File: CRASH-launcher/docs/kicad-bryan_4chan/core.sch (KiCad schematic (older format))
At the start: 22 parts, among them IC501 RFM12B, IC502 ATMEGA328P-PU, K501 CONN_3, K502 CONN_3, K503 CONN_3, P501 CONN_3X2, P502 TTL Serial / Prog, SW501 SW_PUSH, X501 8MHz

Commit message: 
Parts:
- removed L501: ANTENNA, symbol INDUCTOR
- removed SW501: SW_PUSH, symbol SW_PUSH
- added Antenna1: CONN_1, symbol CONN_1
- renumbered C501 to C10, C502 to C11, C503 to C12, C504 to C13, C505 to C14, C506 to C15, D501 to D7, D502 to D8, IC501 to IC1, IC502 to IC2, K501 to K1, K502 to K2, K503 to K3, P501 to P8, P502 to P9, R501 to R47, R502 to R48, R503 to R49, SP501 to SP1, X501 to X1
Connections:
- net labels removed: +3.3V
- no-connect marks 7 -> 6
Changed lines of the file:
@@
-EESchema Schematic File Version 2  date Mon 20 Feb 2012 05:21:35 PM MST
+EESchema Schematic File Version 2  date Sat 05 May 2012 12:12:20 AM MDT
 LIBS:bryan_custom
 LIBS:rfm12
@@
 $Descr User 11000 8500
 encoding utf-8
-Sheet 5 5
+Sheet 6 6
 Title ""
-Date "21 feb 2012"
+Date "13 apr 2012"
 Rev ""
 Comp ""
@@
 $EndDescr
 $Comp
-L SW_PUSH SW501
-U 1 1 4F25DF75
-P 3950 6500
-F 0 "SW501" H 4100 6610 50  0000 C CNN
-F 1 "SW_PUSH" H 3950 6420 50  0000 C CNN
-	1    3950 6500
-	1    0    0    -1
-$EndComp
-$Comp
-L VDD #PWR019
+L VCC #PWR029
+U 1 1 4F87B8EF
+P 5150 1400
+F 0 "#PWR029" H 5150 1500 30  0001 C CNN
+F 1 "VCC" H 5150 1500 30  0000 C CNN
+	1    5150 1400
+	1    0    0    -1
+$EndComp
+$Comp
+L CONN_1 Antenna1
+U 1 1 4F87B8C5
+P 9300 2150
+F 0 "Antenna1" H 9380 2150 40  0000 L CNN
+F 1 "CONN_1" H 9300 2205 30  0001 C CNN
+	1    9300 2150
+	1    0    0    -1
+$EndComp
+$Comp
+L VCC #PWR030
+U 1 1 4F87B852
+P 8100 1550
+F 0 "#PWR030" H 8100 1650 30  0001 C CNN
+F 1 "VCC" H 8100 1650 30  0000 C CNN
+	1    8100 1550
+	1    0    0    -1
+$EndComp
+$Comp
+L VCC #PWR031
+U 1 1 4F87B835
+P 7300 3050
+F 0 "#PWR031" H 7300 3150 30  0001 C CNN
+F 1 "VCC" H 7300 3150 30  0000 C CNN
+	1    7300 3050
+	1    0    0    -1
+$EndComp
+$Comp
+L VCC #PWR032
+U 1 1 4F87B826
+P 1950 3000
+F 0 "#PWR032" H 1950 3100 30  0001 C CNN
+F 1 "VCC" H 1950 3100 30  0000 C CNN
+	1    1950 3000
+	1    0    0    -1
+$EndComp
+$Comp
+L VDD #PWR033
 U 1 1 4F25DACF
 P 6000 4750
-F 0 "#PWR019" H 6000 4850 30  0001 C CNN
+F 0 "#PWR033" H 6000 4850 30  0001 C CNN
 F 1 "VDD" H 6000 4860 30  0000 C CNN
 	1    6000 4750
 	0    -1   -1   0
-$EndComp
-$Comp
-L VDD #PWR020
-U 1 1 4F25DABF
-P 1950 3000
-F 0 "#PWR020" H 1950 3100 30  0001 C CNN
-F 1 "VDD" H 1950 3110 30  0000 C CNN
-	1    1950 3000
-	1    0    0    -1
-$EndComp
-$Comp
-L VDD #PWR021
-U 1 1 4F25DAA5
-P 8100 1550
-F 0 "#PWR021" H 8100 1650 30  0001 C CNN
-F 1 "VDD" H 8100 1660 30  0000 C CNN
-	1    8100 1550
-	1    0    0    -1
-$EndComp
-$Comp
-L VDD #PWR022
-U 1 1 4F25DA9A
-P 7300 3050
-F 0 "#PWR022" H 7300 3150 30  0001 C CNN
-F 1 "VDD" H 7300 3160 30  0000 C CNN
-	1    7300 3050
-	1    0    0    -1
 $EndComp
 Wire Wire Line
@@
 	5850 3500 4250 3500
 $Comp
-L VCC #PWR023
+L VCC #PWR034
 U 1 1 4F25D9CA
 P 7700 6250
-F 0 "#PWR023" H 7700 6350 30  0001 C CNN
+F 0 "#PWR034" H 7700 6350 30  0001 C CNN
 F 1 "VCC" H 7700 6350 30  0000 C CNN
 	1    7700 6250
@@
 $EndComp
 $Comp
-L R R502
+L R R48
 U 1 1 4F25D9BE
 P 7350 6250
-F 0 "R502" H 7380 6310 50  0000 C CNN
+F 0 "R48" H 7380 6310 50  0000 C CNN
 F 1 "47" H 7380 6190 50  0000 C CNN
 	1    7350 6250
@@
 $EndComp
 $Comp
-L C C504
+L C C13
 U 1 1 4F25D964
 P 2150 3800
-F 0 "C504" H 2200 3900 50  0000 L CNN
+F 0 "C13" H 2200 3900 50  0000 L CNN
 F 1 "0.1uF" H 2200 3700 50  0000 L CNN
 	1    2150 3800
@@
 SCK
 $Comp
-L GND #PWR024
+L GND #PWR035
 U 1 1 4E55CA93
 P 7700 6650
-F 0 "#PWR024" H 7700 6650 30  0001 C CNN
+F 0 "#PWR035" H 7700 6650 30  0001 C CNN
 F 1 "GND" H 7700 6580 30  0001 C CNN
 	1    7700 6650
@@
 $EndComp
 $Comp
-L LED D502
+L LED D8
 U 1 1 4E55CA16
 P 6800 6650
-F 0 "D502" H 6800 6750 50  0000 C CNN
+F 0 "D8" H 6800 6750 50  0000 C CNN
 F 1 "LED" H 6800 6550 50  0000 C CNN
 	1    6800 6650
@@
 $EndComp
 $Comp
-L R R503
+L R R49
 U 1 1 4E55C9FC
 P 7350 6650
-F 0 "R503" H 7380 6710 50  0000 C CNN
+F 0 "R49" H 7380 6710 50  0000 C CNN
 F 1 "47" H 7380 6590 50  0000 C CNN
 	1    7350 6650
@@
 $EndComp
 $Comp
-L LED D501
+L LED D7
 U 1 1 4E55C998
 P 6800 6250
-F 0 "D501" H 6800 6350 50  0000 C CNN
+F 0 "D7" H 6800 6350 50  0000 C CNN
 F 1 "LED" H 6800 6150 50  0000 C CNN
 	1    6800 6250
@@
 $EndComp
 $Comp
-L CONN_3 K503
+L CONN_3 K3
 U 1 1 4F1E3C3B
 P 7050 2600
-F 0 "K503" V 7000 2600 50  0000 C CNN
+F 0 "K3" V 7000 2600 50  0000 C CNN
 F 1 "CONN_3" V 7100 2600 40  0000 C CNN
 	1    7050 2600
@@
 $EndComp
 $Comp
-L CONN_3 K501
+L CONN_3 K1
 U 1 1 4F1E3B9E
 P 6100 1000
-F 0 "K501" V 6050 1000 50  0000 C CNN
+F 0 "K1" V 6050 1000 50  0000 C CNN
 F 1 "CONN_3" V 6150 1000 40  0000 C CNN
 	1    6100 1000
@@
 $EndComp
 $Comp
-L CONN_3 K502
+L CONN_3 K2
 U 1 1 4F1E3ACF
 P 5650 1400
-F 0 "K502" V 5600 1400 50  0000 C CNN
+F 0 "K2" V 5600 1400 50  0000 C CNN
 F 1 "CONN_3" V 5700 1400 40  0000 C CNN
 	1    5650 1400
@@
 $EndComp
 $Comp
-L RFM12B IC501
+L RFM12B IC1
 U 1 1 4E48B011
 P 8550 3200
-F 0 "IC501" V 8550 3200 60  0000 C CNN
+F 0 "IC1" V 8550 3200 60  0000 C CNN
 F 1 "RFM12B" H 8944 3594 60  0000 C CNN
 	1    8550 3200
@@
 NoConn ~ 8450 4150
 NoConn ~ 8600 2250
-NoConn ~ 9150 1550
-$Comp
-L C C506
+$Comp
+L C C15
 U 1 1 4E48A3EC
 P 6550 4750
-F 0 "C506" H 6600 4850 50  0000 L CNN
+F 0 "C15" H 6600 4850 50  0000 L CNN
 F 1 "0.1uF" H 6550 4650 50  0000 L CNN
 	1    6550 4750
@@
 $EndComp
 $Comp
-L GND #PWR025
+L GND #PWR036
 U 1 1 4EAB7AD6
 P 7700 2800
-F 0 "#PWR025" H 7700 2800 30  0001 C CNN
+F 0 "#PWR036" H 7700 2800 30  0001 C CNN
 F 1 "GND" H 7700 2730 30  0001 C CNN
 	1    7700 2800
@@
 $EndComp
 $Comp
-L C C501
+L C C10
 U 1 1 4EAB7AD5
 P 7700 3000
-F 0 "C501" H 7750 3100 50  0000 L CNN
+F 0 "C10" H 7750 3100 50  0000 L CNN
 F 1 "0.1uF" H 7750 2900 50  0000 L CNN
 	1    7700 3000
@@
 $EndComp
 $Comp
-L GND #PWR026
+L GND #PWR037
 U 1 1 4EAB7AD4
 P 5850 5050
-F 0 "#PWR026" H 5850 5050 30  0001 C CNN
+F 0 "#PWR037" H 5850 5050 30  0001 C CNN
 F 1 "GND" H 5850 4980 30  0001 C CNN
 	1    5850 5050
@@
 $EndComp
 $Comp
-L CONN_6 P502
+L CONN_6 P9
 U 1 1 4EAB7AD2
 P 6200 5400
-F 0 "P502" V 6200 5400 60  0000 C CNN
+F 0 "P9" V 6200 5400 60  0000 C CNN
 F 1 "TTL Serial / Prog" V 6350 5400 60  0000 C CNN
 	1    6200 5400
@@
 $EndComp
 $Comp
-L INDUCTOR L501
-U 1 1 4EAB7AD1
-P 9150 1850
-F 0 "L501" V 9100 1850 40  0000 C CNN
-F 1 "ANTENNA" V 9250 1850 40  0000 C CNN
-	1    9150 1850
-	1    0    0    -1
-$EndComp
-$Comp
-L GND #PWR027
+L GND #PWR038
 U 1 1 4EAB7AD0
 P 4400 1700
-F 0 "#PWR027" H 4400 1700 30  0001 C CNN
+F 0 "#PWR038" H 4400 1700 30  0001 C CNN
 F 1 "GND" H 4400 1630 30  0001 C CNN
 	1    4400 1700
@@
 $EndComp
 $Comp
-L SPEAKER SP501
+L SPEAKER SP1
 U 1 1 4EAB7ACF
 P 4100 1800
-F 0 "SP501" H 4000 2050 70  0000 C CNN
+F 0 "SP1" H 4000 2050 70  0000 C CNN
 F 1 "SPEAKER" H 4000 1550 70  0000 C CNN
 	1    4100 1800
@@
 $EndComp
 $Comp
-L GND #PWR028
+L GND #PWR039
 U 1 1 4EAB7ACE
 P 7900 1850
-F 0 "#PWR028" H 7900 1850 30  0001 C CNN
+F 0 "#PWR039" H 7900 1850 30  0001 C CNN
 F 1 "GND" H 7900 1780 30  0001 C CNN
 	1    7900 1850
@@
 $EndComp
 $Comp
-L CONN_3X2 P501
+L CONN_3X2 P8
 U 1 1 4E485706
 P 7500 1800
-F 0 "P501" H 7500 2050 50  0000 C CNN
+F 0 "P8" H 7500 2050 50  0000 C CNN
 F 1 "CONN_3X2" V 7500 1850 40  0000 C CNN
 	1    7500 1800
@@
 $EndComp
 $Comp
-L GND #PWR029
+L GND #PWR040
 U 1 1 4E48554A
 P 6250 3800
-F 0 "#PWR029" H 6250 3800 30  0001 C CNN
+F 0 "#PWR040" H 6250 3800 30  0001 C CNN
 F 1 "GND" H 6250 3730 30  0001 C CNN
 	1    6250 3800
@@
 $EndComp
 $Comp
-L C C505
+L C C14
 U 1 1 4EAB7ACA
 P 6050 4100
-F 0 "C505" V 6100 4200 50  0000 L CNN
+F 0 "C14" V 6100 4200 50  0000 L CNN
 F 1 "22pF" V 5950 4200 30  0000 L CNN
 	1    6050 4100
@@
 $EndComp
 $Comp
-L C C503
+L C C12
 U 1 1 4E485523
 P 6050 3500
-F 0 "C503" V 6100 3600 50  0000 L CNN
+F 0 "C12" V 6100 3600 50  0000 L CNN
 F 1 "22pF" V 5950 3600 30  0000 L CNN
 	1    6050 3500
@@
 $EndComp
 $Comp
-L CRYSTAL X501
+L CRYSTAL X1
 U 1 1 4E48548A
 P 5850 3800
-F 0 "X501" V 5850 3900 60  0000 C CNN
+F 0 "X1" V 5850 3900 60  0000 C CNN
 F 1 "8MHz" H 5850 3650 60  0000 C CNN
 F 2 "HC-49" H 5850 3800 60  0001 C CNN
@@
 $EndComp
 $Comp
-L GND #PWR030
+L GND #PWR041
 U 1 1 4E4853B0
 P 9150 3350
-F 0 "#PWR030" H 9150 3350 30  0001 C CNN
+F 0 "#PWR041" H 9150 3350 30  0001 C CNN
 F 1 "GND" H 9150 3280 30  0001 C CNN
 	1    9150 3350
@@
 $EndComp
 $Comp
-L R R501
+L R R47
 U 1 1 4EAB7AC6
 P 5050 1650
-F 0 "R501" H 5080 1710 50  0000 C CNN
+F 0 "R47" H 5080 1710 50  0000 C CNN
 F 1 "10k" H 5080 1590 50  0000 C CNN
 	1    5050 1650
@@
 $EndComp
 $Comp
-L +3.3V #PWR031
-U 1 1 4EAB7AC5
-P 5150 1400
-F 0 "#PWR031" H 5150 1360 30  0001 C CNN
-F 1 "+3.3V" H 5150 1510 30  0000 C CNN
-	1    5150 1400
-	0    1    1    0
-$EndComp
-$Comp
-L GND #PWR032
+L GND #PWR042
 U 1 1 4EAB7AC4
 P 1750 3800
-F 0 "#PWR032" H 1750 3800 30  0001 C CNN
+F 0 "#PWR042" H 1750 3800 30  0001 C CNN
 F 1 "GND" H 1750 3730 30  0001 C CNN
 	1    1750 3800
@@
 $EndComp
 $Comp
-L C C502
+L C C11
 U 1 1 4EAB7AC3
 P 1950 3400
-F 0 "C502" H 2000 3500 50  0000 L CNN
+F 0 "C11" H 2000 3500 50  0000 L CNN
 F 1 "0.1uF" H 2000 3300 50  0000 L CNN
 	1    1950 3400
@@
 $EndComp
 $Comp
-L GND #PWR033
+L GND #PWR043
 U 1 1 4E4848A6
 P 2350 5300
-F 0 "#PWR033" H 2350 5300 30  0001 C CNN
+F 0 "#PWR043" H 2350 5300 30  0001 C CNN
 F 1 "GND" H 2350 5230 30  0001 C CNN
 	1    2350 5300
@@
 $EndComp
 $Comp
-L ATMEGA328P-P IC502
+L ATMEGA328P-P IC2
 U 1 1 4E4842AA
 P 3250 4000
-F 0 "IC502" H 2550 5250 50  0000 L BNN
+F 0 "IC2" H 2550 5250 50  0000 L BNN
 F 1 "ATMEGA328P-PU" H 3450 2600 50  0000 L BNN
 F 2 "DIL28" H 2650 2650 50  0001 C CNN

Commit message: first REAL shot at PCB
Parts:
- added SW1: SW_PUSH, symbol SW_PUSH
- C11, C12, C13, C14, C15: footprint (none) -> C2
- K1: footprint (none) -> SIL-3
- P16: renamed from P9; footprint (none) -> PIN_ARRAY-6X1
- renumbered P8 to P15, R47 to R7, R48 to R8, R49 to R9
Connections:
- net labels added: ADC_CS, GPIO_CS
- net labels removed: VCC
- wire segments 93 -> 91
- no-connect marks 6 -> 13

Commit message: second try at PCB layout.  this one might actually work!
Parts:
- removed SP1: SPEAKER, symbol SPEAKER
- added D10, D9: LED, symbol LED
- added P21: SIREN_A, symbol CONN_2
- added P22: SIREN_B, symbol CONN_2
- added Q1, Q2: NPN, symbol NPN
- added R12, R13: 47, symbol R
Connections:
- net ADC_CS: now also IC2.26 ((PCINT11/ADC3)PC3); no longer IC2.12 ((PCINT22/OC0A/AIN0)PD6)
- net GND: now also P21.1 (P1), P22.1 (P1), Q1.1 (E), Q2.1 (E)
- net GPIO_CS: now also IC2.25 ((PCINT10/ADC2)PC2); no longer IC2.13 ((PCINT23/AIN1)PD7)
- net MISO: now also IC1.1 (SDO), K2.1 (P1); no longer IC2.18 ((PCINT4/MISO)PB4), K2.2 (PM)
- net MOSI: now also IC1.12 (SDI), K3.1 (P1); no longer IC2.17 ((PCINT3/OC2A/MOSI)PB3), K3.2 (PM)
- net SCK: now also IC1.13 (SCK), K1.1 (P1); no longer IC2.19 ((PCINT5/SCK)PB5), K1.2 (PM)
- net VDD: now also R12.2, R13.1
- net at IC2.14 ((PCINT0/CLKO/ICP1)PB0): now also P21.2 (PM)
- net at IC2.15 ((PCINT1/OC1A)PB1): now also P22.2 (PM)
- net at IC2.2 ((PCINT16/RXD)PD0), P16.5: now also Q2.2 (B)
- net at IC2.3 ((PCINT17/TXD)PD1), P16.4: now also Q1.2 (B)
- net GPIO_RESET: now reaches IC2.6 ((PCINT20/XCK/T0)PD4)
- new net: IC2.17 ((PCINT3/OC2A/MOSI)PB3), K3.2 (PM)
- new net: IC2.18 ((PCINT4/MISO)PB4), K2.2 (PM)
- new net: IC2.19 ((PCINT5/SCK)PB5), K1.2 (PM)
- new net: D10.2 (K), Q2.3 (C)
- new net: D10.1 (A), R13.2
- new net: D9.2 (K), Q1.3 (C)
- new net: D9.1 (A), R12.1
- no-connect marks 13 -> 11
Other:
- moved on the sheet: C15, P16, SW1

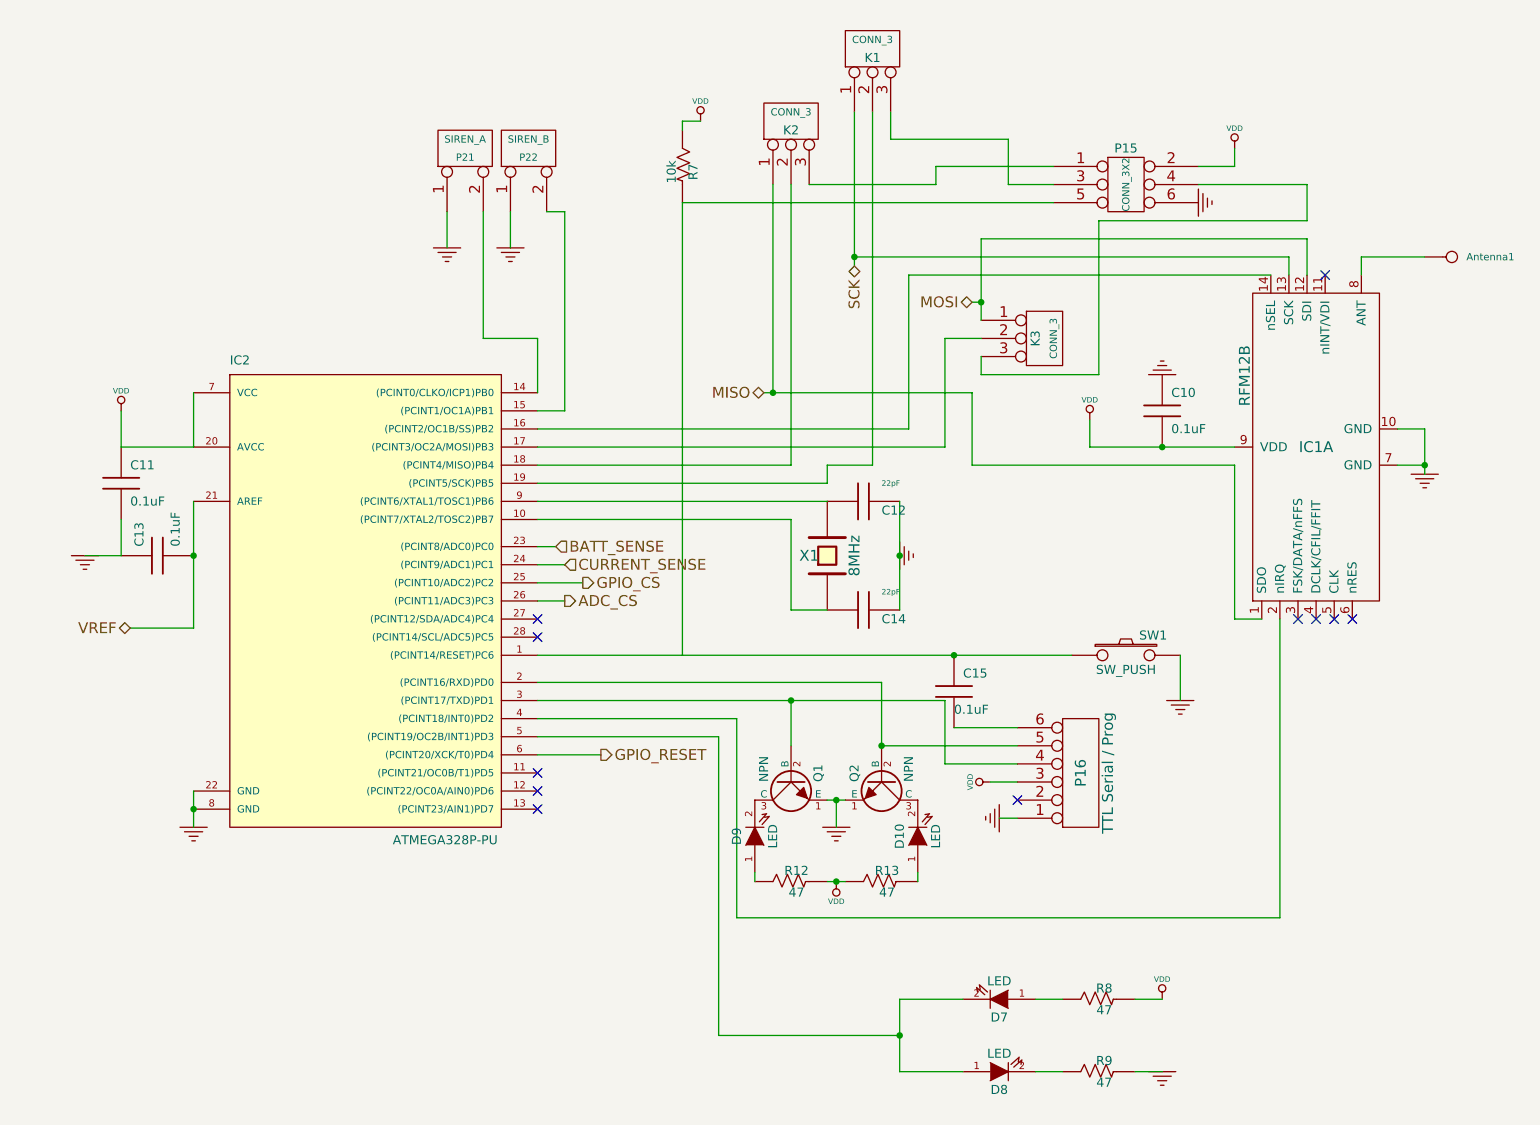
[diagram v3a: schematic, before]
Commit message: further refined PCB, it has safety switch and fire switch and lots of errors fixed!
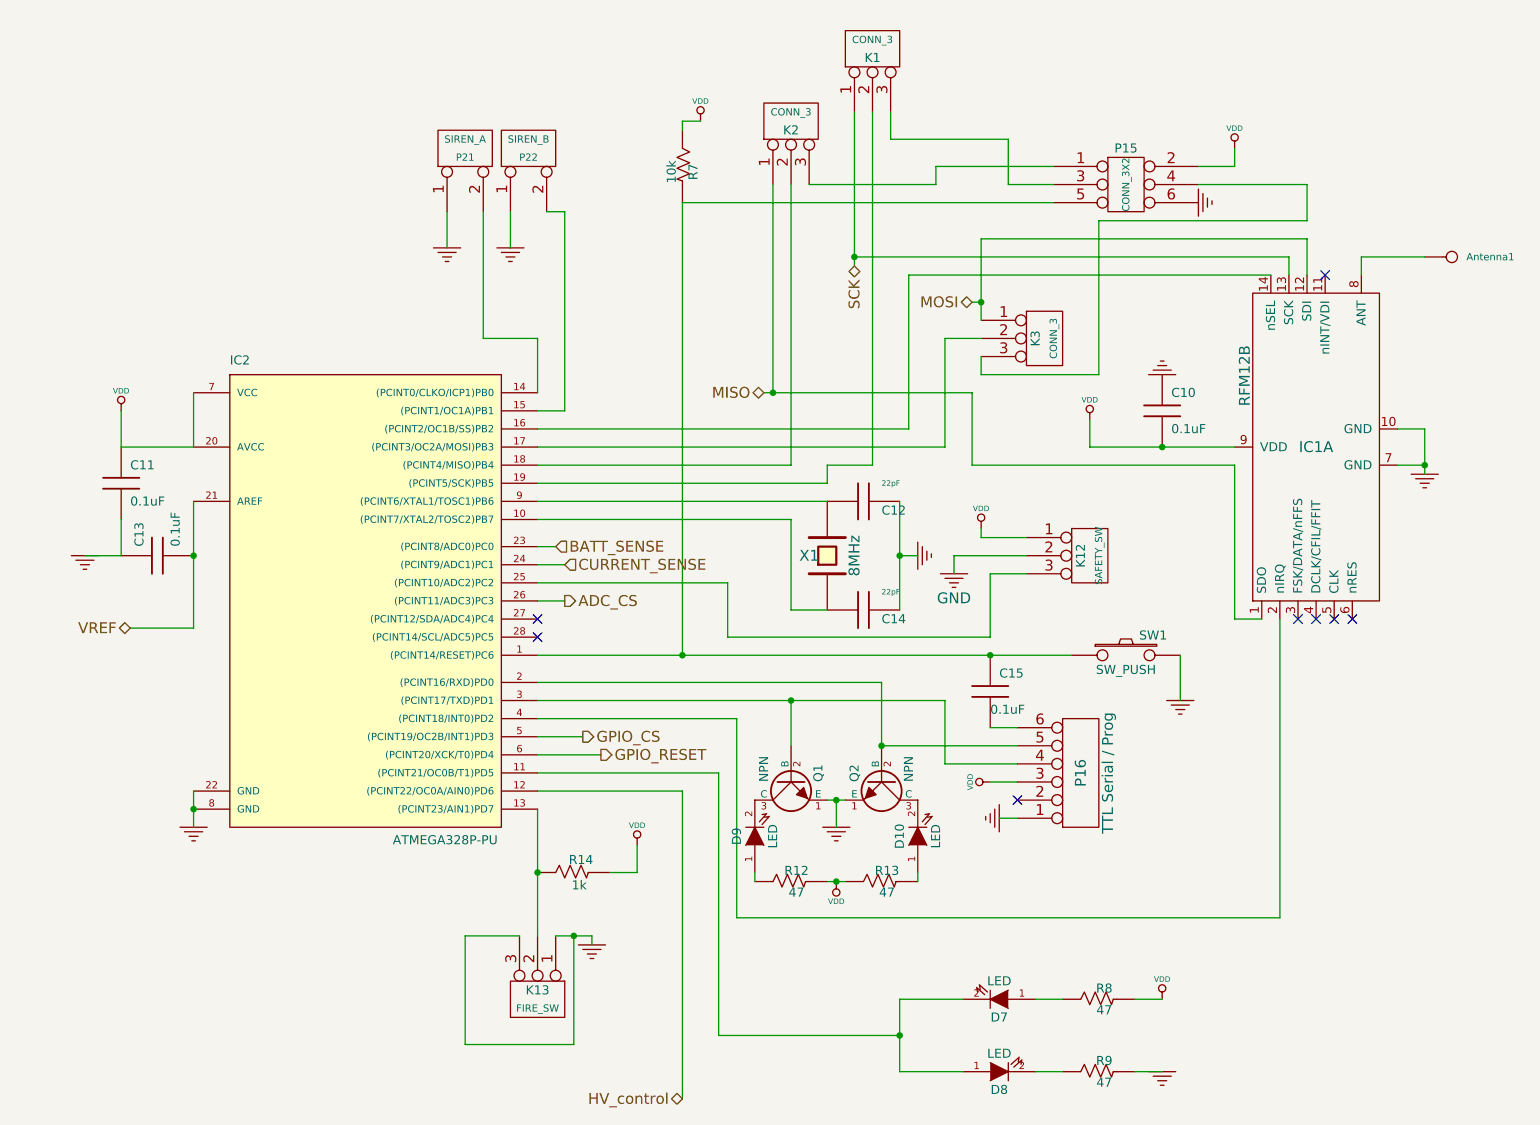
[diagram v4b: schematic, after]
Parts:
- added K12: SAFETY_SW, symbol CONN_3
- added K13: FIRE_SW, symbol CONN_3
- added R14: 1k, symbol R
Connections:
- net GND: now also K12.2 (PM), K13.1 (P1), K13.3 (P3)
- net GPIO_CS: now also IC2.5 ((PCINT19/OC2B/INT1)PD3); no longer IC2.25 ((PCINT10/ADC2)PC2)
- net VDD: now also K12.1 (P1), R14.2
- net at C15.1, IC2.1 ((PCINT14/RESET)PC6), SW1.1: now also P15.5, R7.2
- net at IC2.11 ((PCINT21/OC0B/T1)PD5): now also D7.2 (K), D8.1 (A)
- net HV_control: now reaches IC2.12 ((PCINT22/OC0A/AIN0)PD6)
- net at IC2.13 ((PCINT23/AIN1)PD7): now also K13.2 (PM), R14.1
- new net: IC2.25 ((PCINT10/ADC2)PC2), K12.3 (P3)
- no-connect marks 11 -> 8
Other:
- moved on the sheet: C15
